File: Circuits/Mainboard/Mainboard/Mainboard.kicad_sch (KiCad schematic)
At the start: 2 parts, among them J1 XT60PW-M, J2 XT60PW-M

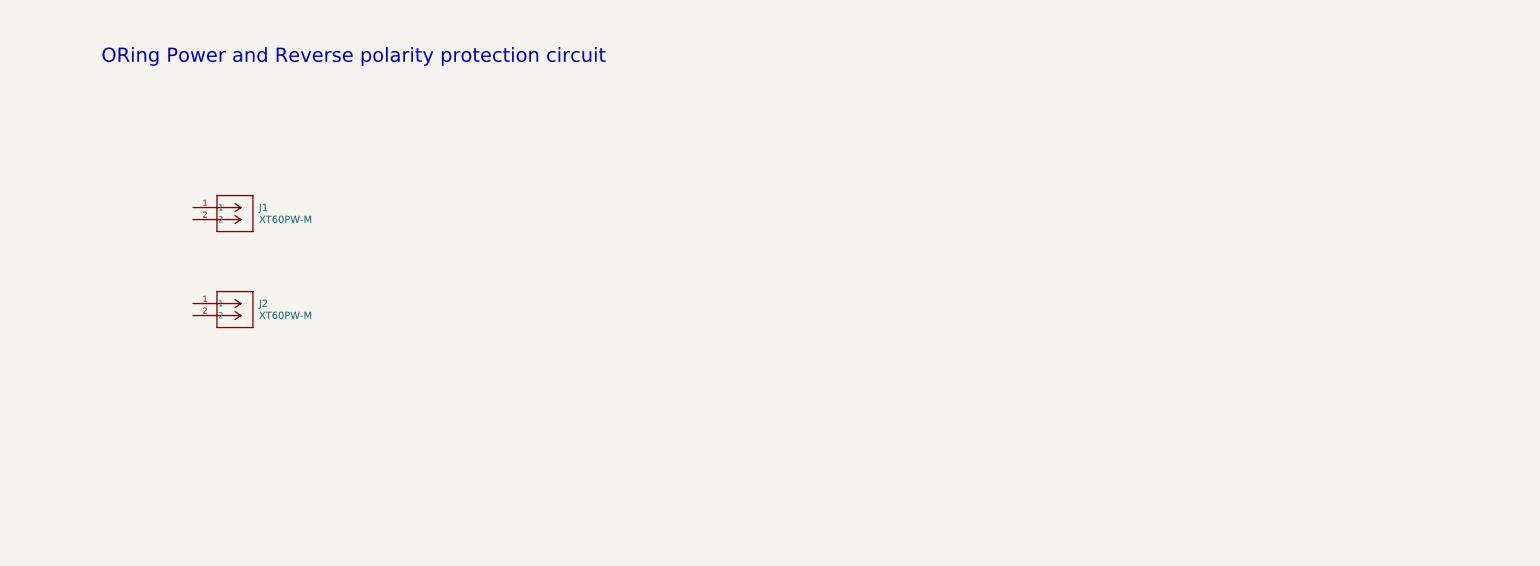
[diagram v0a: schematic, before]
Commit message: Added all ORing components and reverse voltage protection components
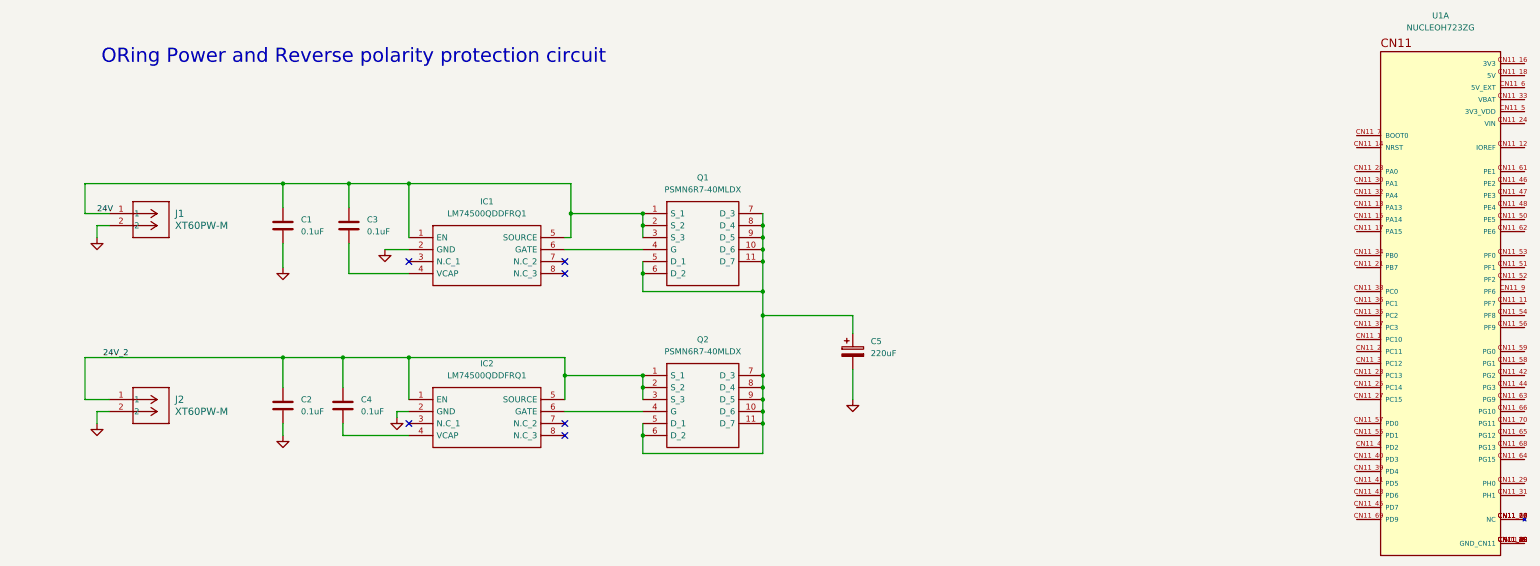
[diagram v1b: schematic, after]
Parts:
- added C1, C2, C3, C4: 0.1uF, symbol Device:C
- added C5: 220uF, symbol Device:C_Polarized
- added IC1, IC2: LM74500QDDFRQ1, LM74500QDDFRQ1:SOT65P280X110-8N, symbol LM74500QDDFRQ1:LM74500QDDFRQ1
- added Q1, Q2: PSMN6R7-40MLDX, PSMN6R740MLDX:PSMN6R740MLDX, symbol PSMN6R7-40MLDX:PSMN6R7-40MLDX
- added U1: NUCLEOH723ZG, NUCLEOH723ZG:MODULE_NUCLEOH723ZG, symbol NUCLEO-H723ZG:NUCLEOH723ZG
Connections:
- net 24V_2: now reaches J2.1
- net 24V_2: now also C2.1, C4.1, IC2.1 (EN), IC2.5 (SOURCE), Q2.1 (S_1), Q2.2 (S_2), Q2.3 (S_3)
- net GND: now reaches J2.2
- net GND: now also J1.2, C1.2, C2.2, C5.2, IC1.2 (GND), IC2.2 (GND)
- net 24V: now reaches J1.1
- net 24V: now also C1.1, C3.1, IC1.1 (EN), IC1.5 (SOURCE), Q1.1 (S_1), Q1.2 (S_2), Q1.3 (S_3)
- new net: C4.2, IC2.4 (VCAP)
- new net: IC2.6 (GATE), Q2.4 (G)
- new net: U1.CN11_10 (NC), U1.CN11_26 (NC), U1.CN11_67 (NC)
- new net: U1.CN11_19 (GND_CN11), U1.CN11_20 (GND_CN11), U1.CN11_22 (GND_CN11), U1.CN11_49 (GND_CN11), U1.CN11_60 (GND_CN11), U1.CN11_8 (GND_CN11)
- new net: C3.2, IC1.4 (VCAP)
- new net: C5.1, Q1.10 (D_6), Q1.11 (D_7), Q1.5 (D_1), Q1.6 (D_2), Q1.7 (D_3), Q1.8 (D_4), Q1.9 (D_5), Q2.10 (D_6), Q2.11 (D_7), Q2.5 (D_1), Q2.6 (D_2), Q2.7 (D_3), Q2.8 (D_4), Q2.9 (D_5)
- new net: IC1.6 (GATE), Q1.4 (G)
- no-connect marks 0 -> 6
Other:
- moved on the sheet: J1, J2

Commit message: Added components that we will use on the mainboard to kicad
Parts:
- added C10, C11, C9: 10uF, Capacitor_SMD:C_0805_2012Metric, symbol Device:C
- added C6, C7, C8: 0.1uF, Capacitor_SMD:C_0805_2012Metric, symbol Device:C
- added IC3: WSEN-ISDS 6-Dof IMU, WSEN-ISDS:2536030320001, symbol WSDN-ISDS:2536030320001
- added IC4: SX1280IMLTRT, SX1280IMLTRT:QFN50P400X400X100-25N-D, symbol SX1280IMLTRT:SX1280IMLTRT
- added IC5: SKY66122-11, SKY66122-11:QFN50P400X400X100-25N-D, symbol SKY66122-11:SKY66122-11
- added PS1: 3.3V Step down, 173010335, symbol WPME-FDSM:173010335
- added PS2: 5V Step down, 173010542, symbol FDSM 5V:173010542
- added PS3: 12V Step down, 173011235, symbol FDSM 12V:173011235
- added R1, R2: 10, Resistor_SMD:R_0805_2012Metric, symbol Device:R
- added U2, U3, U4, U5, U6: B-G431B-ESC1, B-G431B-ESC1:B-G431B-ESC1_MOUNT, symbol B-G431B-ESC1:B-G431B-ESC1
- C1, C3: footprint (none) -> Capacitor_SMD:C_0805_2012Metric_Pad1.18x1.45mm_HandSolder
- C2, C4, C5: footprint (none) -> Capacitor_SMD:C_0805_2012Metric
- J1, J2: footprint CONN_XT60PW-M_AMA -> XT60PW-M:CONN_XT60PW-M_AMA
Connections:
- net 24V: now also C5.1, Q1.10 (D_6), Q1.11 (D_7), Q1.5 (D_1), Q1.6 (D_2), Q1.7 (D_3), Q1.8 (D_4), Q1.9 (D_5), Q2.10 (D_6), Q2.11 (D_7), Q2.5 (D_1), Q2.6 (D_2), Q2.7 (D_3), Q2.8 (D_4), Q2.9 (D_5), C10.1, C11.1, C6.1, C7.1, C8.1, C9.1, PS1.1 (VIN), PS2.1 (VIN), PS3.1 (VIN); no longer C1.1, C3.1, IC1.1 (EN), IC1.5 (SOURCE), J1.1, Q1.1 (S_1), Q1.2 (S_2), Q1.3 (S_3)
- net GND: now also C10.2, C11.2, C6.2, C7.2, C8.2, C9.2, PS1.2 (GND), PS2.2 (GND), PS3.2 (GND)
- net at IC2.6 (GATE): now also R2.2; no longer Q2.4 (G)
- net at Q1.4 (G): now also R1.1; no longer IC1.6 (GATE)
- new net: IC1.6 (GATE), R1.2
- new net: Q2.4 (G), R2.1
- new net 12V: PS3.3 (VOUT)
- new net 24V_1: C1.1, C3.1, IC1.1 (EN), IC1.5 (SOURCE), J1.1, Q1.1 (S_1), Q1.2 (S_2), Q1.3 (S_3)
- new net 3.3V: PS1.3 (VOUT)
- new net 5V: PS2.3 (VOUT)
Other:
- moved on the sheet: C1, C2, C3, C4, C5, IC1, IC2, J1, J2, Q1, Q2, U1A

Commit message: Added headers in the circuit for the mainboard in kicad
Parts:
- added J3: Conn_01x02_Pin, symbol Connector:Conn_01x02_Pin
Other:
- moved on the sheet: U1A, U2, U3, U4, U5, U6
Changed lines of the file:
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@@
 	(symbol
 		(lib_id "NUCLEO-H723ZG:NUCLEOH723ZG")
-		(at 373.38 157.48 0)
+		(at 356.87 144.78 0)
 		(unit 1)
 		(exclude_from_sim no)
@@
 		(fields_autoplaced yes)
 		(property "Reference" "U1"
-			(at 373.38 96.52 0)
+			(at 356.87 83.82 0)
 			(effects
 				(font
@@
 		)
 		(property "Value" "NUCLEOH723ZG"
-			(at 373.38 99.06 0)
+			(at 356.87 86.36 0)
 			(effects
 				(font
@@
 		)
 		(property "Footprint" "NUCLEOH723ZG:MODULE_NUCLEOH723ZG"
-			(at 373.38 157.48 0)
+			(at 356.87 144.78 0)
 			(effects
 				(font
@@
 		)
 		(property "Datasheet" ""
-			(at 373.38 157.48 0)
+			(at 356.87 144.78 0)
 			(effects
 				(font
@@
 		)
 		(property "Description" ""
-			(at 373.38 157.48 0)
+			(at 356.87 144.78 0)
 			(effects
 				(font
@@
 		)
 		(property "MF" "STMicroelectronics"
-			(at 373.38 157.48 0)
+			(at 356.87 144.78 0)
 			(effects
 				(font
@@
 		)
 		(property "MAXIMUM_PACKAGE_HEIGHT" "18.57 mm"
-			(at 373.38 157.48 0)
+			(at 356.87 144.78 0)
 			(effects
 				(font
@@
 		)
 		(property "Package" "None"
-			(at 373.38 157.48 0)
+			(at 356.87 144.78 0)
 			(effects
 				(font
@@
 		)
 		(property "Price" "None"
-			(at 373.38 157.48 0)
+			(at 356.87 144.78 0)
 			(effects
 				(font
@@
 		)
 		(property "Check_prices" "https://www.snapeda.com/parts/NUCLEOH723ZG/STMicroelectronics/view-part/?ref=eda"
-			(at 373.38 157.48 0)
+			(at 356.87 144.78 0)
 			(effects
 				(font
@@
 		)
 		(property "STANDARD" "Manufacturer Recommendations"
-			(at 373.38 157.48 0)
+			(at 356.87 144.78 0)
 			(effects
 				(font
@@
 		)
 		(property "PARTREV" "2"
-			(at 373.38 157.48 0)
+			(at 356.87 144.78 0)
 			(effects
 				(font
@@
 		)
 		(property "SnapEDA_Link" "https://www.snapeda.com/parts/NUCLEOH723ZG/STMicroelectronics/view-part/?ref=snap"
-			(at 373.38 157.48 0)
+			(at 356.87 144.78 0)
 			(effects
 				(font
@@
 		)
 		(property "MP" "NUCLEOH723ZG"
-			(at 373.38 157.48 0)
+			(at 356.87 144.78 0)
 			(effects
 				(font
@@
 		)
 		(property "Purchase-URL" "https://www.snapeda.com/api/url_track_click_mouser/?unipart_id=8820245&manufacturer=STMicroelectronics&part_name=NUCLEOH723ZG&search_term=None"
-			(at 373.38 157.48 0)
+			(at 356.87 144.78 0)
 			(effects
 				(font
@@
 		)
 		(property "Description_1" "\nSTM32H723 Nucleo-144 STM32H7 ARM® Cortex®-M7 MCU 32-Bit Embedded Evaluation Board\n"
-			(at 373.38 157.48 0)
+			(at 356.87 144.78 0)
 			(effects
 				(font
@@
 		)
 		(property "SNAPEDA_PN" "NUCLEOH723ZG"
-			(at 373.38 157.48 0)
+			(at 356.87 144.78 0)
 			(effects
 				(font
@@
 		)
 		(property "Availability" "In Stock"
-			(at 373.38 157.48 0)
+			(at 356.87 144.78 0)
 			(effects
 				(font
@@
 		)
 		(property "MANUFACTURER" "STMicroelectronics"
-			(at 373.38 157.48 0)
+			(at 356.87 144.78 0)
 			(effects
 				(font
@@
 	(symbol
 		(lib_id "B-G431B-ESC1:B-G431B-ESC1")
-		(at 256.54 49.53 0)
+		(at 458.47 124.46 0)
 		(unit 1)
 		(exclude_from_sim no)
@@
 		(fields_autoplaced yes)
 		(property "Reference" "U6"
-			(at 256.54 35.56 0)
+			(at 458.47 110.49 0)
 			(effects
 				(font
@@
 		)
 		(property "Value" "B-G431B-ESC1"
-			(at 256.54 38.1 0)
+			(at 458.47 113.03 0)
 			(effects
 				(font
@@
 		)
 		(property "Footprint" "B-G431B-ESC1:B-G431B-ESC1_MOUNT"
-			(at 254 49.53 0)
+			(at 455.93 124.46 0)
 			(effects
 				(font
@@
 		)
 		(property "Datasheet" ""
-			(at 254 49.53 0)
+			(at 455.93 124.46 0)
 			(effects
 				(font
@@
 		)
 		(property "Description" ""
-			(at 256.54 49.53 0)
+			(at 458.47 124.46 0)
 			(effects
 				(font
@@
 	)
 	(symbol
+		(lib_id "Connector:Conn_01x02_Pin")
+		(at 78.74 186.69 0)
+		(unit 1)
+		(exclude_from_sim no)
+		(in_bom yes)
+		(on_board yes)
+		(dnp no)
+		(fields_autoplaced yes)
+		(property "Reference" "J3"
+			(at 79.375 181.61 0)
+			(effects
+				(font
+					(size 1.27 1.27)
+				)
+			)
+		)
+		(property "Value" "Conn_01x02_Pin"
+			(at 79.375 184.15 0)
+			(effects
+				(font
+					(size 1.27 1.27)
+				)
+			)
+		)
+		(property "Footprint" ""
+			(at 78.74 186.69 0)
+			(effects
+				(font
+					(size 1.27 1.27)
+				)
+				(hide yes)
+			)
+		)
+		(property "Datasheet" "~"
+			(at 78.74 186.69 0)
+			(effects
+				(font
+					(size 1.27 1.27)
+				)
+				(hide yes)
+			)
+		)
+		(property "Description" "Generic connector, single row, 01x02, script generated"
+			(at 78.74 186.69 0)
+			(effects
+				(font
+					(size 1.27 1.27)
+				)
+				(hide yes)
+			)
+		)
+		(pin "2"
+		)
+		(pin "1"
+		)
+		(instances
+			(project ""
+				(path "/778a7f39-1f28-457f-badd-61056e9c01e2"
+					(reference "J3")
+					(unit 1)
+				)
+			)
+		)
+	)
+	(symbol
 		(lib_id "WPME-FDSM:173010335")
 		(at 227.33 118.11 0)
@@
 	(symbol
 		(lib_id "B-G431B-ESC1:B-G431B-ESC1")
-		(at 283.21 73.66 0)
+		(at 485.14 148.59 0)
 		(unit 1)
 		(exclude_from_sim no)
@@
 		(fields_autoplaced yes)
 		(property "Reference" "U4"
-			(at 283.21 59.69 0)
+			(at 485.14 134.62 0)
 			(effects
 				(font
@@
 		)
 		(property "Value" "B-G431B-ESC1"
-			(at 283.21 62.23 0)
+			(at 485.14 137.16 0)
 			(effects
 				(font
@@
 		)
 		(property "Footprint" "B-G431B-ESC1:B-G431B-ESC1_MOUNT"
-			(at 280.67 73.66 0)
+			(at 482.6 148.59 0)
 			(effects
 				(font
@@
 		)
 		(property "Datasheet" ""
-			(at 280.67 73.66 0)
+			(at 482.6 148.59 0)
 			(effects
 				(font
@@
 		)
 		(property "Description" ""
-			(at 283.21 73.66 0)
+			(at 485.14 148.59 0)
 			(effects
 				(font
@@
 	(symbol
 		(lib_id "B-G431B-ESC1:B-G431B-ESC1")
-		(at 311.15 49.53 0)
+		(at 513.08 124.46 0)
 		(unit 1)
 		(exclude_from_sim no)
@@
 		(fields_autoplaced yes)
 		(property "Reference" "U3"
-			(at 311.15 35.56 0)
+			(at 513.08 110.49 0)
 			(effects
 				(font
@@
 		)
 		(property "Value" "B-G431B-ESC1"
-			(at 311.15 38.1 0)
+			(at 513.08 113.03 0)
 			(effects
 				(font
@@
 		)
 		(property "Footprint" "B-G431B-ESC1:B-G431B-ESC1_MOUNT"
-			(at 308.61 49.53 0)
+			(at 510.54 124.46 0)
 			(effects
 				(font
@@
 		)
 		(property "Datasheet" ""
-			(at 308.61 49.53 0)
+			(at 510.54 124.46 0)
 			(effects
 				(font
@@
 		)
 		(property "Description" ""
-			(at 311.15 49.53 0)
+			(at 513.08 124.46 0)
 			(effects
 				(font
@@
 	(symbol
 		(lib_id "B-G431B-ESC1:B-G431B-ESC1")
-		(at 283.21 49.53 0)
+		(at 485.14 124.46 0)
 		(unit 1)
 		(exclude_from_sim no)
@@
 		(fields_autoplaced yes)
 		(property "Reference" "U2"
-			(at 283.21 35.56 0)
+			(at 485.14 110.49 0)
 			(effects
 				(font
@@
 		)
 		(property "Value" "B-G431B-ESC1"
-			(at 283.21 38.1 0)
+			(at 485.14 113.03 0)
 			(effects
 				(font
@@
 		)
 		(property "Footprint" "B-G431B-ESC1:B-G431B-ESC1_MOUNT"
-			(at 280.67 49.53 0)
+			(at 482.6 124.46 0)
 			(effects
 				(font
@@
 		)
 		(property "Datasheet" ""
-			(at 280.67 49.53 0)
+			(at 482.6 124.46 0)
 			(effects
 				(font
@@
 		)
 		(property "Description" ""
-			(at 283.21 49.53 0)
+			(at 485.14 124.46 0)
 			(effects
 				(font
@@
 	(symbol
 		(lib_id "B-G431B-ESC1:B-G431B-ESC1")
-		(at 311.15 73.66 0)
+		(at 513.08 148.59 0)
 		(unit 1)
 		(exclude_from_sim no)
@@
 		(fields_autoplaced yes)
 		(property "Reference" "U5"
-			(at 311.15 59.69 0)
+			(at 513.08 134.62 0)
 			(effects
 				(font
@@
 		)
 		(property "Value" "B-G431B-ESC1"
-			(at 311.15 62.23 0)
+			(at 513.08 137.16 0)
 			(effects
 				(font
@@
 		)
 		(property "Footprint" "B-G431B-ESC1:B-G431B-ESC1_MOUNT"
-			(at 308.61 73.66 0)
+			(at 510.54 148.59 0)
 			(effects
 				(font
@@
 		)
 		(property "Datasheet" ""
-			(at 308.61 73.66 0)
+			(at 510.54 148.59 0)
 			(effects
 				(font
@@
 		)
 		(property "Description" ""
-			(at 311.15 73.66 0)
+			(at 513.08 148.59 0)
 			(effects
 				(font

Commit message: Removed unused components and added the rest of the nucleo to kicad schematic
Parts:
- removed J3: Conn_01x02_Pin, symbol Connector:Conn_01x02_Pin
- added C12, C13, C14: 0.1uF, Capacitor_SMD:C_0805_2012Metric, symbol Device:C
- added J3: Conn_01x07_Pin, symbol Connector:Conn_01x07_Pin
- added J4, J9: Conn_01x05_Pin, symbol Connector:Conn_01x05_Pin
- added J8: Conn_01x06_Pin, symbol Connector:Conn_01x06_Pin
- added unit 5 of U1
- added unit 9 of U1
- added unit 6 of U1
- added unit 3 of U1
- added unit 4 of U1
- added unit 2 of U1
- added unit 7 of U1
- added unit 10 of U1
- added unit 8 of U1
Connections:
- net 3.3V: now also U1.CN11_16 (3V3), C12.1, C13.1, C14.1, J3.1 (Pin_1), J4.1 (Pin_1), J8.1 (Pin_1), U1.CN8_7 (3V3_CN8), U1.CN8_8 (D46/SDMMC_D3)
- net GND: now also U1.CN11_19 (GND_CN11), U1.CN11_20 (GND_CN11), U1.CN11_22 (GND_CN11), U1.CN11_49 (GND_CN11), U1.CN11_60 (GND_CN11), U1.CN11_8 (GND_CN11), C12.2, C13.2, C14.2, J3.3 (Pin_3), J4.2 (Pin_2), J8.2 (Pin_2), U1.CN10_17 (GND_CN10), U1.CN10_22 (GND_CN10), U1.CN10_27 (GND_CN10), U1.CN10_5 (GND_CN10), U1.CN12_20 (GND_CN12), U1.CN12_32 (AGND_CN12), U1.CN12_39 (GND_CN12), U1.CN12_54 (GND_CN12), U1.CN12_63 (GND_CN12), U1.CN12_9 (GND_CN12), U1.CN15_1 (GND_CN15), U1.CN15_2 (GND_CN15), U1.CN16_1 (GND_CN16), U1.CN16_2 (GND_CN16), U1.CN3_1 (GND_CN3), U1.CN3_2 (GND_CN3), U1.CN4_1 (GND_CN4), U1.CN4_2 (GND_CN4), U1.CN7_8 (GND_CN7), U1.CN8_11 (GND_CN8), U1.CN8_12 (D48/SDMMC_CMD), U1.CN8_13 (GND_CN8), U1.CN8_14 (D49/IO), U1.CN9_12 (GND_CN9), U1.CN9_23 (GND_CN9)
- new net BNO055_BL-IND: J9.4 (Pin_4)
- new net BNO055_Boot: J9.1 (Pin_1)
- new net BNO055_INT: J4.5 (Pin_5)
- new net BNO055_PS1: J9.2 (Pin_2)
- new net BNO055_PS2: J9.3 (Pin_3)
- new net BNO055_RST: J9.5 (Pin_5)
- new net BNO055_SCL: J4.3 (Pin_3)
- new net BNO055_SDA: J4.4 (Pin_4)
- new net VL53L1_INT: J8.5 (Pin_5)
- new net VL53L1_SCL: J8.4 (Pin_4)
- new net VL53L1_SDA: J8.3 (Pin_3)
- new net VL53L1_SHUT: J8.6 (Pin_6)
- new net VL6180_GPIO: J3.4 (Pin_4)
- new net VL6180_SCL: J3.6 (Pin_6)
- new net VL6180_SDA: J3.7 (Pin_7)
- new net VL6180_SHDN: J3.5 (Pin_5)
- no-connect marks 6 -> 11
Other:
- note added: "BNO055"
- note added: "TOF400C-VL53L1"
- note added: "VL6180 TOF"
- moved on the sheet: IC3, IC4, IC5, U1A, U2, U3, U4, U5, U6

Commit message: Added 3D models for the pcb components
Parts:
- removed PS1: 3.3V Step down, 173010335, symbol WPME-FDSM:173010335
- removed U2, U3, U4, U5, U6: B-G431B-ESC1, B-G431B-ESC1:B-G431B-ESC1_MOUNT, symbol B-G431B-ESC1:B-G431B-ESC1
- added C15, C17: 100nF, Capacitor_SMD:C_0805_2012Metric, symbol Device:C
- added C16, C18: 1nF, Capacitor_SMD:C_0805_2012Metric, symbol Device:C
- added C19: 1uF, Capacitor_SMD:C_0805_2012Metric, symbol Device:C
- added C20, C21: 10nF, Capacitor_SMD:C_0805_2012Metric, symbol Device:C
- added C22: 470uF, Capacitor_SMD:C_0805_2012Metric, symbol Device:C_Polarized
- added C23: 0.1uF, Capacitor_SMD:C_0805_2012Metric, symbol Device:C
- added D1: D_Schottky, symbol Device:D_Schottky
- added IC6: TS2596CM533_RNG, TS2596CM533_RNG:TS2596CM550RNG, symbol TS2596CM533_RNG:TS2596CM533_RNG
- added J5: B6B-PH-K-S, B6B-PH-K-S:JST_B6B-PH-K-S, symbol B6B-PH-K-S:B6B-PH-K-S
- added J6: B5P-VH_LF__SN_, B5P-VH-LF-SN:B5P-VH_LF__SN_, symbol B5P-VH-LF-SN:B5P-VH_LF__SN_
- added L2: AMRM00101040470MA1, AMRM00101040470MA1:AMRM00101040470MA1, symbol AMRM00101040470MA1:AMRM00101040470MA1
- J4: footprint (none) -> Connector_PinHeader_1.00mm:PinHeader_1x05_P1.00mm_Vertical
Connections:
- net 24V: now also IC6.1 (INPUT)
- net 3.3V: now also IC4.15 (VBAT), C15.1, C16.1, C17.1, C18.1, C22.1, C23.1, IC6.4 (FEEDBACK), L2.2; no longer C12.1, U1.CN11_16 (3V3)
- net GND: now also IC4.13 (GND_2), IC4.20 (GND_3), IC4.21 (GND_4), IC4.23 (GND_5), IC4.24 (GND_6), IC4.5 (GND_1), C15.2, C16.2, C17.2, C18.2, C19.2, C20.2, C21.2, C22.2, C23.2, D1.2 (A), IC6.3 (GND_1), IC6.5 (ENABLE), IC6.6 (GND_2)
- net at IC4.1 (VR_PA): now also C21.1
- net at IC4.12 (DCC_FB): now also IC4.2 (VDD_IN), C19.1, C20.1
- new net: D1.1 (K), IC6.2 (SW_OUTPUT), L2.1
- new net: C12.1, U1.CN11_16 (3V3)
- no-connect marks 11 -> 15
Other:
- note added: "Hall sensor connector"
- note added: "Motor Connector"
- moved on the sheet: C12, IC4, U1A
